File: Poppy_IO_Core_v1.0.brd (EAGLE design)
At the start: 67.6 x 31.8 mm, 101 parts, among them IC3 ATMEGA2560-16AU, IC6 LP2985-33DBVR, Q1 16MHz, Q2 16MHz, Q3 16MHz, Q4 16MHz, Q5 24MHz, U1 ATmega16u2, U2 MPU-6000, U3 USB2514B-AEZC, U4 ATmega16u2, U5 ATmega16u2, X1 1376408-SLOT_1.8V

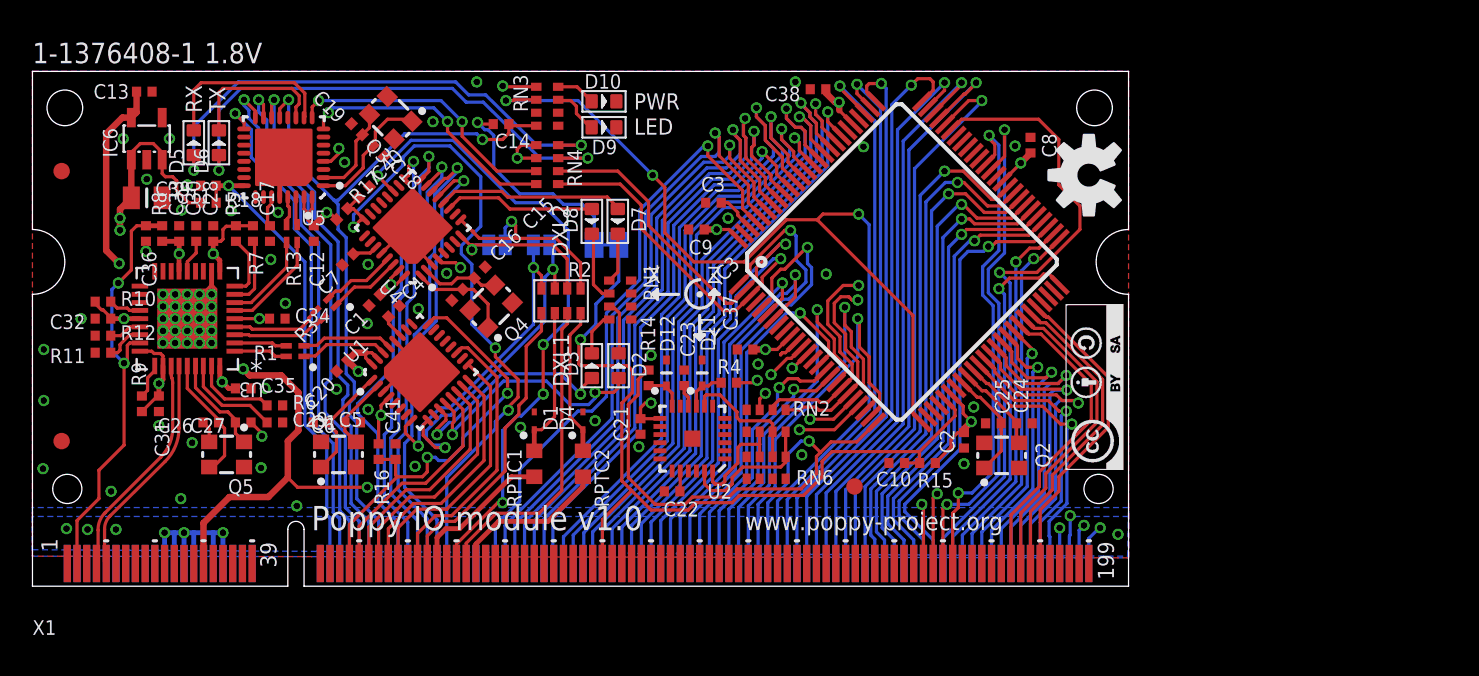
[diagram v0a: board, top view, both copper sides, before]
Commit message: Some cosmetic adjustment so that it looks as supposed in circuithub: - removed names and values from the board to hide them (no way to hide the layer!) - removed all solder paste on the back
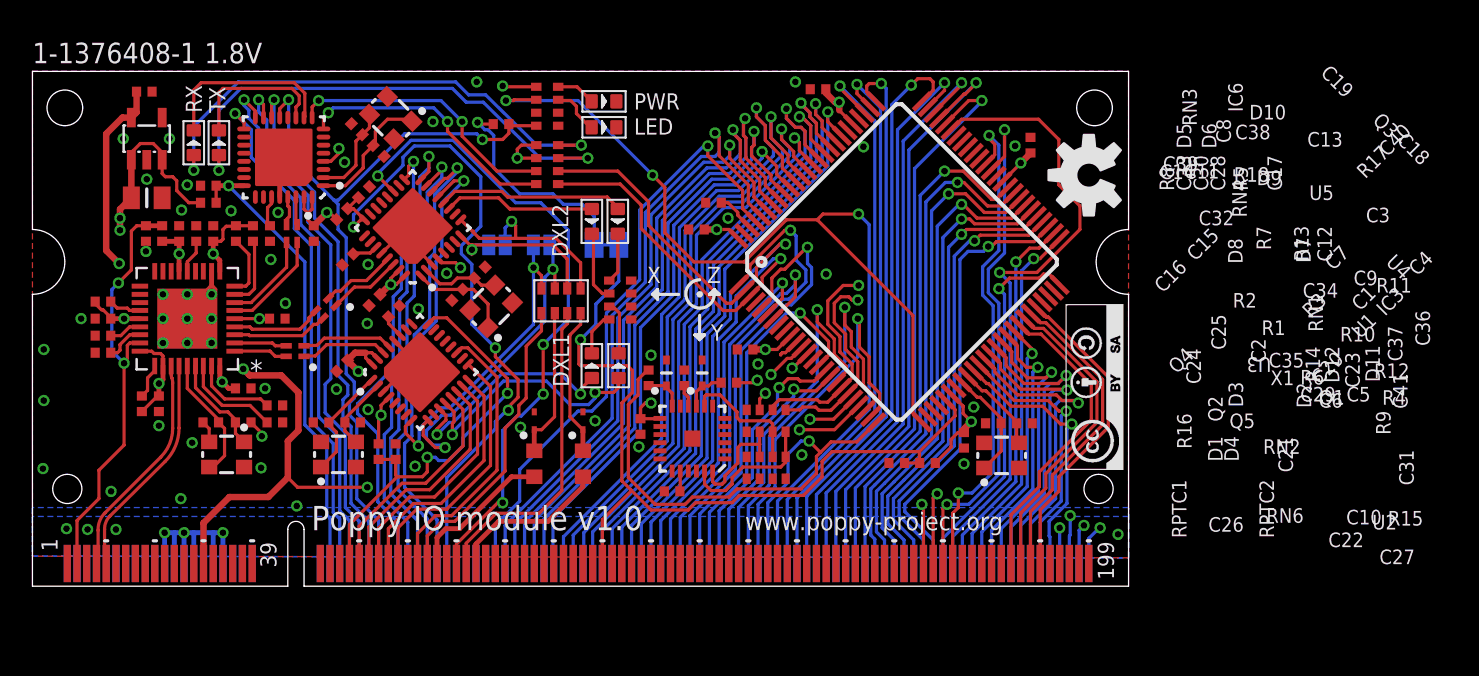
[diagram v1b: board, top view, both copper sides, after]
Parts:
- removed FD1, FD2, FD3: FIDUCIALMOUNT, SmartPrj:FIDUCIA-MOUNT
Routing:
- net GND: vias 72 -> 56
